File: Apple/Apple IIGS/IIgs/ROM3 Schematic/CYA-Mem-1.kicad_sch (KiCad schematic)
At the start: 38 parts, among them J20 IIgs_Memory_Connector, U6 65SC816

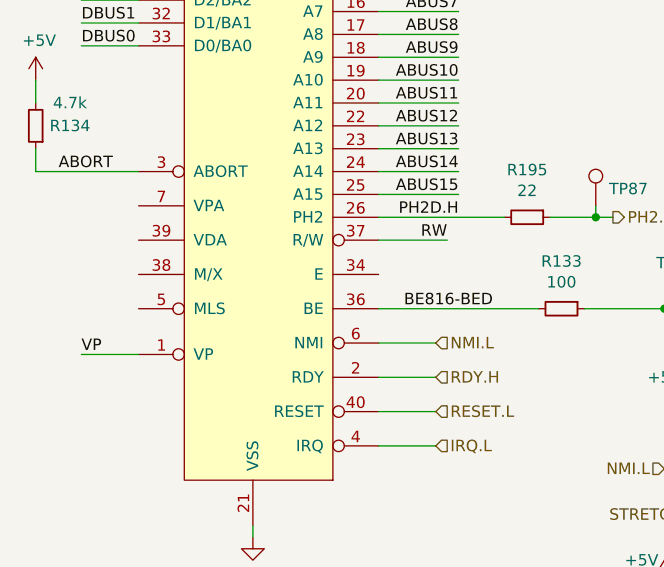
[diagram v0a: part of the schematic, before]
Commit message: 399 ERC, Rescue symbol clean-up
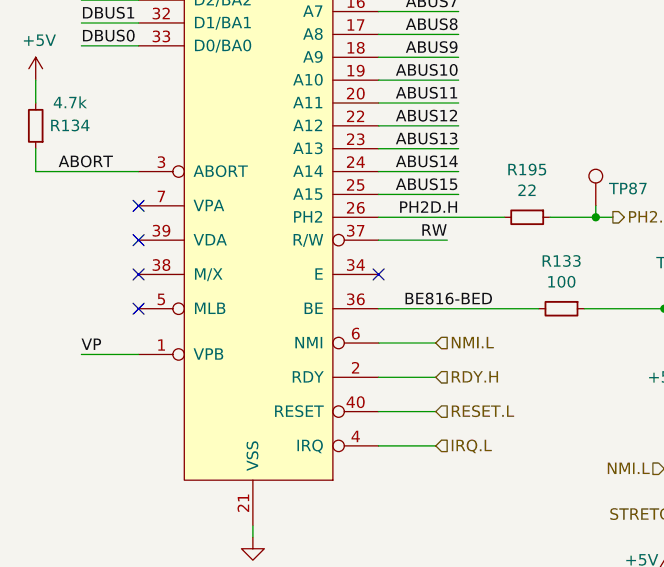
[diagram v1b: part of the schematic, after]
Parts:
- C62: symbol IIgs-Schematic-rescue:CP_Small-Device -> Device:C_Polarized_Small
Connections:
- no-connect marks 0 -> 5
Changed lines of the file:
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@@
   (junction (at 213.36 163.83) (diameter 0) (color 0 0 0 0)
   )
+  (no_connect (at 92.71 129.54))
+  (no_connect (at 119.38 137.16))
+  (no_connect (at 92.71 137.16))
+  (no_connect (at 92.71 140.97))
+  (no_connect (at 92.71 133.35))
   (bus_entry (at 359.41 71.12) (size -2.54 2.54)
     (stroke (width 0) (type default) (color 0 0 0 0))
@@
     (pin "1")
   )
-  (symbol (lib_id "IIgs-Schematic-rescue:CP_Small-Device") (at 160.02 191.77 0) (unit 1)
+  (symbol (lib_id "Device:C_Polarized_Small") (at 160.02 191.77 0) (unit 1)
     (in_bom yes) (on_board yes)
     (property "Reference" "C62" (id 0) (at 162.2552 190.6016 0)
@@
       (effects (font (size 1.27 1.27)) (justify left))
     )
-    (property "Footprint" "" (id 2) (at 160.9852 195.58 0)
-      (effects (font (size 1.27 1.27)) hide)
-    )
+    (property "Footprint" "" (id 2) (at 160.02 191.77 0)
+      (effects (font (size 1.27 1.27)) hide)
+    )

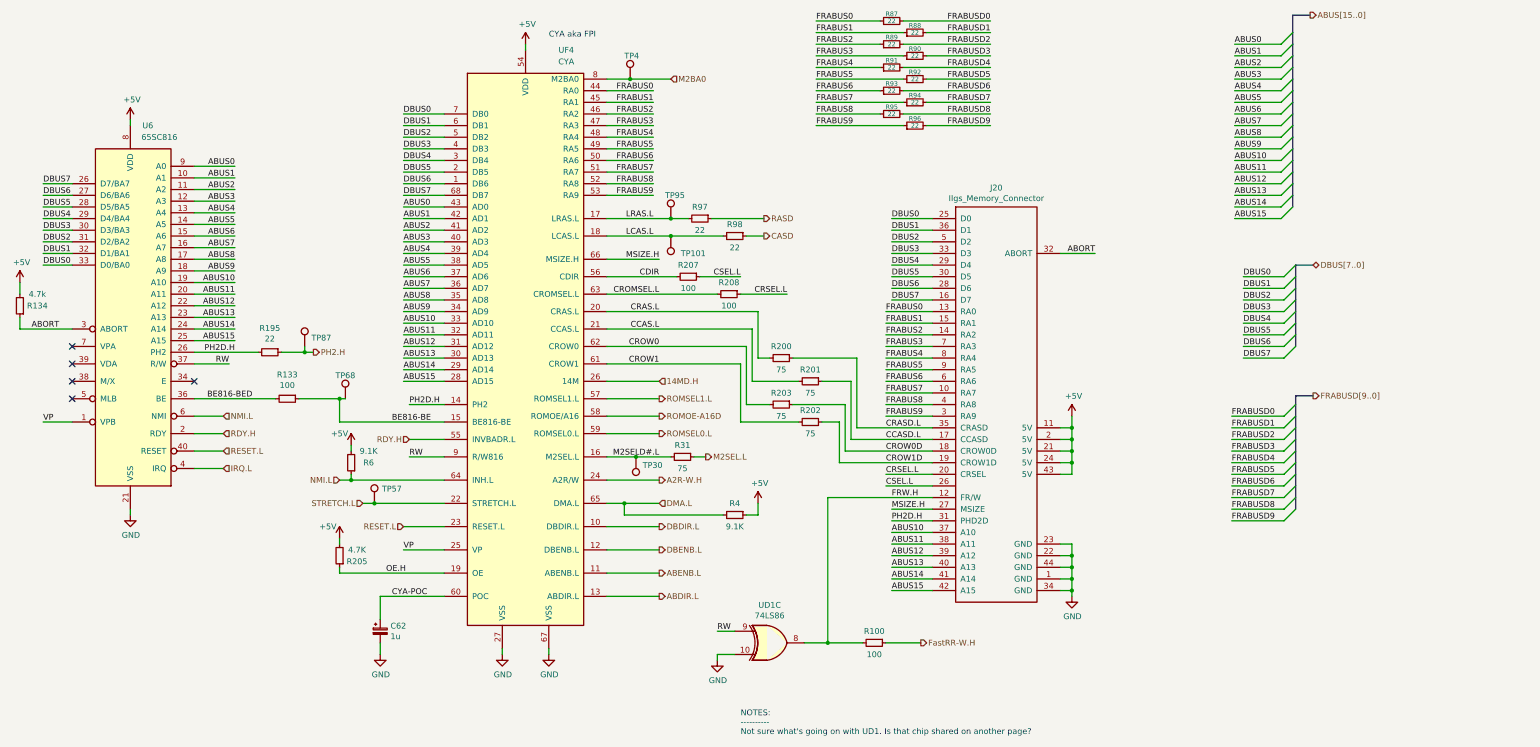
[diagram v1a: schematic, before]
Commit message: moved v5 version to separate directory
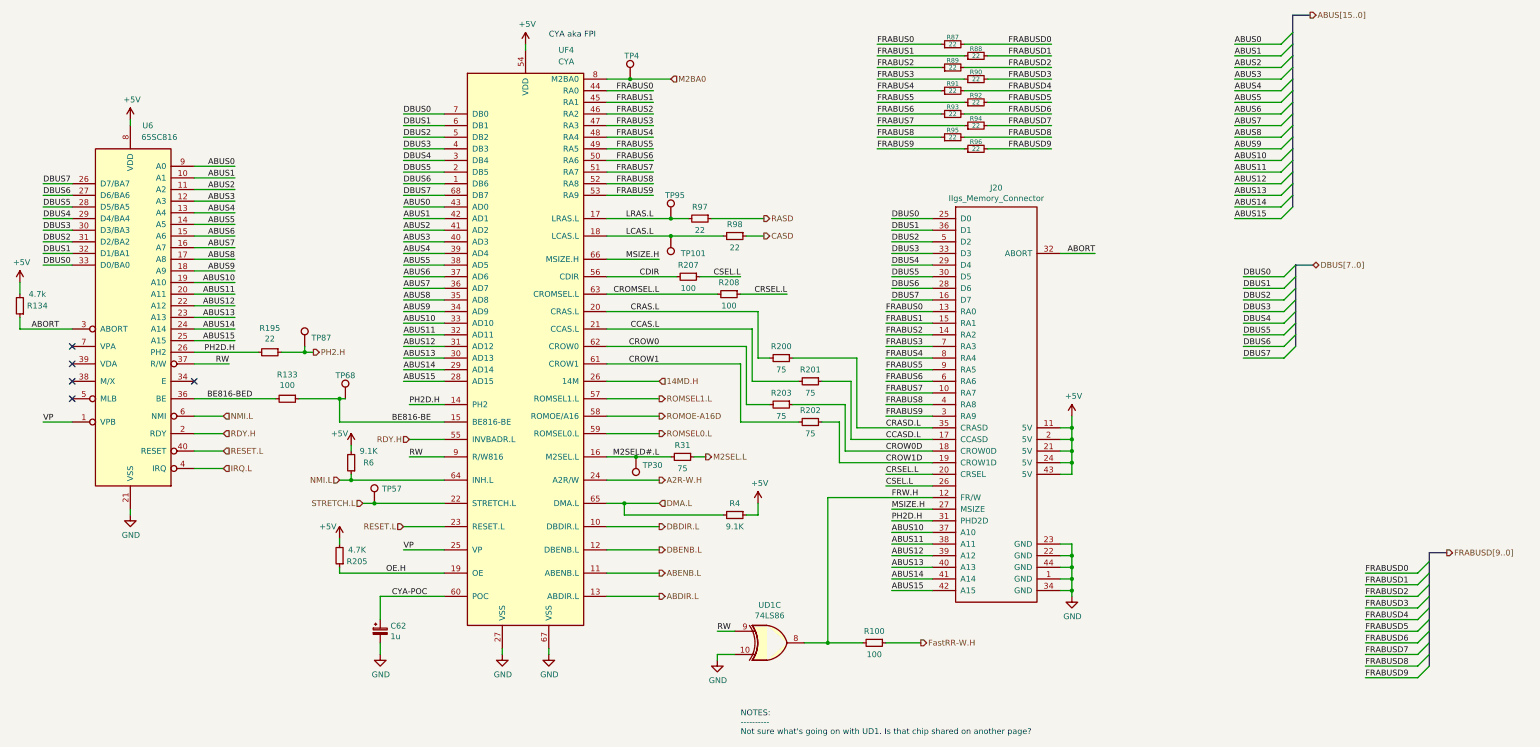
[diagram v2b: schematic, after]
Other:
- moved on the sheet: R87, R88, R89, R90, R91, R92, R93, R94, R95, R96

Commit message: 0 ERC Errors AND Warnings. Whew. ICs updated with correct pin assignments and many (many) other fixes.
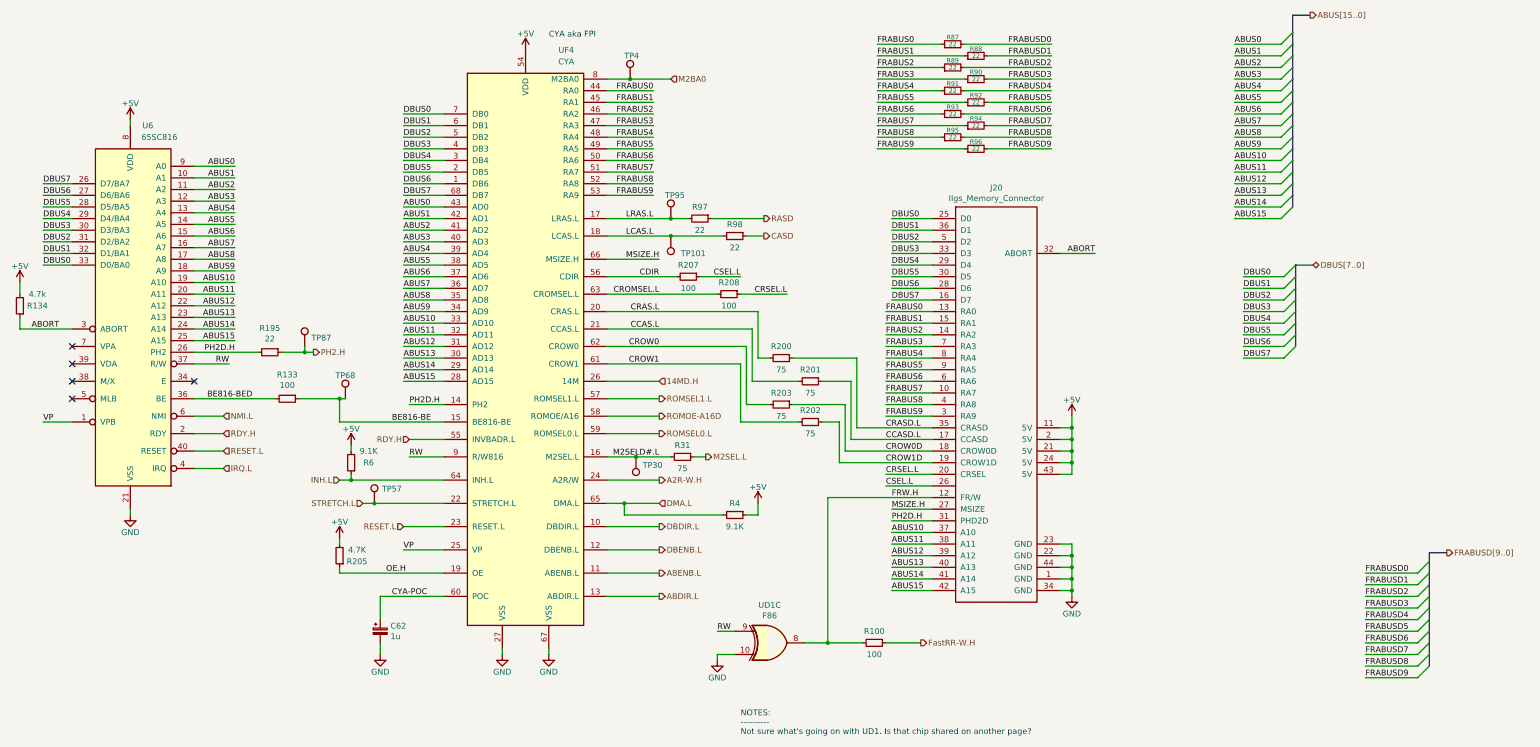
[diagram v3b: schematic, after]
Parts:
- UD1: value 74LS86 -> F86
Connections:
- net NMI.L: no longer R6.1, UF4.64 (INH.L)
- new net INH.L: R6.1, UF4.64 (INH.L)
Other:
- title: (none) -> CPU and Fast Memory Controller (CYA)
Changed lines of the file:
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@@
   (paper "A3")
   (title_block
+    (title "CPU and Fast Memory Controller (CYA)")
     (rev "2")
     (company "bald.ee/bitpreserve")
@@
     (stroke (width 0) (type default) (color 0 0 0 0))
   )
+  (wire (pts (xy 196.85 195.58) (xy 196.85 196.85))
+    (stroke (width 0) (type default) (color 0 0 0 0))
+  )
   (wire (pts (xy 173.99 142.24) (xy 166.37 142.24))
     (stroke (width 0) (type default) (color 0 0 0 0))
@@
     (stroke (width 0) (type default) (color 0 0 0 0))
   )
-  (wire (pts (xy 196.85 195.58) (xy 196.85 196.85))
-    (stroke (width 0) (type default) (color 0 0 0 0))
-  )
   (wire (pts (xy 138.43 130.81) (xy 143.51 130.81))
     (stroke (width 0) (type default) (color 0 0 0 0))
@@
     (stroke (width 0) (type default) (color 0 0 0 0))
   )
+  (wire (pts (xy 186.69 195.58) (xy 186.69 196.85))
+    (stroke (width 0) (type default) (color 0 0 0 0))
+  )
   (wire (pts (xy 81.28 125.73) (xy 92.71 125.73))
     (stroke (width 0) (type default) (color 0 0 0 0))
@@
     (stroke (width 0) (type default) (color 0 0 0 0))
   )
-  (wire (pts (xy 186.69 195.58) (xy 186.69 196.85))
-    (stroke (width 0) (type default) (color 0 0 0 0))
-  )
   (wire (pts (xy 311.15 180.34) (xy 311.15 182.88))
     (stroke (width 0) (type default) (color 0 0 0 0))
@@
   )
   (wire (pts (xy 209.55 73.66) (xy 219.71 73.66))
-    (stroke (width 0) (type default) (color 0 0 0 0))
-  )
-  (wire (pts (xy 191.77 63.5) (xy 191.77 64.77))
     (stroke (width 0) (type default) (color 0 0 0 0))
   )
@@
     (effects (font (size 1.27 1.27)) (justify left))
   )
-  (hierarchical_label "NMI.L" (shape input) (at 151.13 158.75 180) (fields_autoplaced)
+  (hierarchical_label "INH.L" (shape input) (at 151.13 158.75 180) (fields_autoplaced)
     (effects (font (size 1.27 1.27)) (justify right))
   )
@@
   (symbol (lib_id "power:GND") (at 105.41 166.37 0) (unit 1)
     (in_bom yes) (on_board yes)
-    (property "Reference" "#PWR0106" (id 0) (at 105.41 172.72 0)
-      (effects (font (size 1.27 1.27)) hide)
-    )
-    (property "Value" "GND" (id 1) (at 105.537 170.7642 0))
+    (property "Reference" "#PWR0113" (id 0) (at 105.41 172.72 0)
+      (effects (font (size 1.27 1.27)) hide)
+    )
+    (property "Value" "GND" (id 1) (at 105.41 170.18 0))
     (property "Footprint" "" (id 2) (at 105.41 166.37 0)
       (effects (font (size 1.27 1.27)) hide)
@@
   (symbol (lib_id "power:+5V") (at 105.41 80.01 0) (unit 1)
     (in_bom yes) (on_board yes)
-    (property "Reference" "#PWR0107" (id 0) (at 105.41 83.82 0)
-      (effects (font (size 1.27 1.27)) hide)
-    )
-    (property "Value" "+5V" (id 1) (at 105.791 75.6158 0))
+    (property "Reference" "#PWR0105" (id 0) (at 105.41 83.82 0)
+      (effects (font (size 1.27 1.27)) hide)
+    )
+    (property "Value" "+5V" (id 1) (at 105.41 76.454 0))
     (property "Footprint" "" (id 2) (at 105.41 80.01 0)
       (effects (font (size 1.27 1.27)) hide)
@@
   (symbol (lib_id "power:+5V") (at 81.28 115.57 0) (unit 1)
     (in_bom yes) (on_board yes)
-    (property "Reference" "#PWR0105" (id 0) (at 81.28 119.38 0)
-      (effects (font (size 1.27 1.27)) hide)
-    )
-    (property "Value" "+5V" (id 1) (at 81.661 111.1758 0))
+    (property "Reference" "#PWR0107" (id 0) (at 81.28 119.38 0)
+      (effects (font (size 1.27 1.27)) hide)
+    )
+    (property "Value" "+5V" (id 1) (at 81.28 112.014 0))
     (property "Footprint" "" (id 2) (at 81.28 115.57 0)
       (effects (font (size 1.27 1.27)) hide)
@@
   (symbol (lib_id "power:+5V") (at 153.67 151.13 0) (unit 1)
     (in_bom yes) (on_board yes)
-    (property "Reference" "#PWR0103" (id 0) (at 153.67 154.94 0)
-      (effects (font (size 1.27 1.27)) hide)
-    )
-    (property "Value" "+5V" (id 1) (at 151.13 148.59 0))
+    (property "Reference" "#PWR0109" (id 0) (at 153.67 154.94 0)
+      (effects (font (size 1.27 1.27)) hide)
+    )
+    (property "Value" "+5V" (id 1) (at 153.67 147.574 0))
     (property "Footprint" "" (id 2) (at 153.67 151.13 0)
       (effects (font (size 1.27 1.27)) hide)
@@
   (symbol (lib_id "power:GND") (at 160.02 196.85 0) (unit 1)
     (in_bom yes) (on_board yes)
-    (property "Reference" "#PWR0112" (id 0) (at 160.02 203.2 0)
-      (effects (font (size 1.27 1.27)) hide)
-    )
-    (property "Value" "GND" (id 1) (at 160.147 201.2442 0))
+    (property "Reference" "#PWR0111" (id 0) (at 160.02 203.2 0)
+      (effects (font (size 1.27 1.27)) hide)
+    )
+    (property "Value" "GND" (id 1) (at 160.02 200.66 0))
     (property "Footprint" "" (id 2) (at 160.02 196.85 0)
       (effects (font (size 1.27 1.27)) hide)
@@
   (symbol (lib_id "power:+5V") (at 151.13 171.45 0) (unit 1)
     (in_bom yes) (on_board yes)
-    (property "Reference" "#PWR0104" (id 0) (at 151.13 175.26 0)
-      (effects (font (size 1.27 1.27)) hide)
-    )
-    (property "Value" "+5V" (id 1) (at 148.59 168.91 0))
+    (property "Reference" "#PWR0108" (id 0) (at 151.13 175.26 0)
+      (effects (font (size 1.27 1.27)) hide)
+    )
+    (property "Value" "+5V" (id 1) (at 151.13 167.894 0))
     (property "Footprint" "" (id 2) (at 151.13 171.45 0)
       (effects (font (size 1.27 1.27)) hide)
@@
     (pin "1")
   )
-  (symbol (lib_id "power:GND") (at 186.69 196.85 0) (unit 1)
-    (in_bom yes) (on_board yes)
-    (property "Reference" "#PWR0111" (id 0) (at 186.69 203.2 0)
-      (effects (font (size 1.27 1.27)) hide)
-    )
-    (property "Value" "GND" (id 1) (at 186.817 201.2442 0))
-    (property "Footprint" "" (id 2) (at 186.69 196.85 0)
-      (effects (font (size 1.27 1.27)) hide)
-    )
-    (property "Datasheet" "" (id 3) (at 186.69 196.85 0)
-      (effects (font (size 1.27 1.27)) hide)
-    )
-    (pin "1")
-  )
   (symbol (lib_id "power:GND") (at 196.85 196.85 0) (unit 1)
     (in_bom yes) (on_board yes)
-    (property "Reference" "#PWR0110" (id 0) (at 196.85 203.2 0)
-      (effects (font (size 1.27 1.27)) hide)
-    )
-    (property "Value" "GND" (id 1) (at 196.977 201.2442 0))
+    (property "Reference" "#PWR0106" (id 0) (at 196.85 203.2 0)
+      (effects (font (size 1.27 1.27)) hide)
+    )
+    (property "Value" "GND" (id 1) (at 196.85 200.66 0))
     (property "Footprint" "" (id 2) (at 196.85 196.85 0)
       (effects (font (size 1.27 1.27)) hide)
@@
   (symbol (lib_id "power:+5V") (at 242.57 163.83 0) (unit 1)
     (in_bom yes) (on_board yes)
-    (property "Reference" "#PWR0108" (id 0) (at 242.57 167.64 0)
-      (effects (font (size 1.27 1.27)) hide)
-    )
-    (property "Value" "+5V" (id 1) (at 242.951 159.4358 0))
+    (property "Reference" "#PWR0103" (id 0) (at 242.57 167.64 0)
+      (effects (font (size 1.27 1.27)) hide)
+    )
+    (property "Value" "+5V" (id 1) (at 242.57 160.274 0))
     (property "Footprint" "" (id 2) (at 242.57 163.83 0)
       (effects (font (size 1.27 1.27)) hide)
@@
       (effects (font (size 1.27 1.27)) hide)
     )
-    (property "Value" "GND" (id 1) (at 311.277 188.5442 0))
+    (property "Value" "GND" (id 1) (at 311.15 187.96 0))
     (property "Footprint" "" (id 2) (at 311.15 184.15 0)
       (effects (font (size 1.27 1.27)) hide)
@@
       (effects (font (size 1.27 1.27)) hide)
     )
-    (property "Value" "+5V" (id 1) (at 311.531 140.3858 0))
+    (property "Value" "+5V" (id 1) (at 311.15 141.224 0))
     (property "Footprint" "" (id 2) (at 311.15 144.78 0)
       (effects (font (size 1.27 1.27)) hide)
@@
     (in_bom yes) (on_board yes)
     (property "Reference" "UD1" (id 0) (at 245.11 186.055 0))
-    (property "Value" "74LS86" (id 1) (at 245.11 188.3664 0))
+    (property "Value" "F86" (id 1) (at 245.11 188.3664 0))
     (property "Footprint" "" (id 2) (at 245.11 194.31 0)
       (effects (font (size 1.27 1.27)) hide)
@@
   (symbol (lib_id "power:GND") (at 233.68 198.12 0) (unit 1)
     (in_bom yes) (on_board yes)
-    (property "Reference" "#PWR0113" (id 0) (at 233.68 204.47 0)
-      (effects (font (size 1.27 1.27)) hide)
-    )
-    (property "Value" "GND" (id 1) (at 233.807 202.5142 0))
+    (property "Reference" "#PWR0112" (id 0) (at 233.68 204.47 0)
+      (effects (font (size 1.27 1.27)) hide)
+    )
+    (property "Value" "GND" (id 1) (at 233.68 201.93 0))
     (property "Footprint" "" (id 2) (at 233.68 198.12 0)
       (effects (font (size 1.27 1.27)) hide)
@@
     (pin "1")
   )
-  (symbol (lib_id "power:+5V") (at 191.77 63.5 0) (unit 1)
-    (in_bom yes) (on_board yes)
-    (property "Reference" "#PWR0109" (id 0) (at 191.77 67.31 0)
-      (effects (font (size 1.27 1.27)) hide)
-    )
-    (property "Value" "+5V" (id 1) (at 192.151 59.1058 0))
-    (property "Footprint" "" (id 2) (at 191.77 63.5 0)
-      (effects (font (size 1.27 1.27)) hide)
-    )
-    (property "Datasheet" "" (id 3) (at 191.77 63.5 0)
+  (symbol (lib_id "power:+5V") (at 191.77 64.77 0) (unit 1)
+    (in_bom yes) (on_board yes)
+    (property "Reference" "#PWR0104" (id 0) (at 191.77 68.58 0)
+      (effects (font (size 1.27 1.27)) hide)
+    )
+    (property "Value" "+5V" (id 1) (at 191.77 61.214 0))
+    (property "Footprint" "" (id 2) (at 191.77 64.77 0)
+      (effects (font (size 1.27 1.27)) hide)
+    )
+    (property "Datasheet" "" (id 3) (at 191.77 64.77 0)
       (effects (font (size 1.27 1.27)) hide)
     )
@@
     (pin "2")
   )
+  (symbol (lib_id "power:GND") (at 186.69 196.85 0) (unit 1)
+    (in_bom yes) (on_board yes)
+    (property "Reference" "#PWR0110" (id 0) (at 186.69 203.2 0)
+      (effects (font (size 1.27 1.27)) hide)
+    )
+    (property "Value" "GND" (id 1) (at 186.69 200.66 0))
+    (property "Footprint" "" (id 2) (at 186.69 196.85 0)
+      (effects (font (size 1.27 1.27)) hide)
+    )
+    (property "Datasheet" "" (id 3) (at 186.69 196.85 0)
+      (effects (font (size 1.27 1.27)) hide)
+    )
+    (pin "1")
+  )
   (symbol (lib_id "Device:R_Small") (at 290.195 81.28 90) (unit 1)
